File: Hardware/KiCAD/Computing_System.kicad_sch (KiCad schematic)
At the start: 7 parts, among them IC9 PCF8575PWR, J1 SD_Card, U1 ESP32-C3-WROOM-02

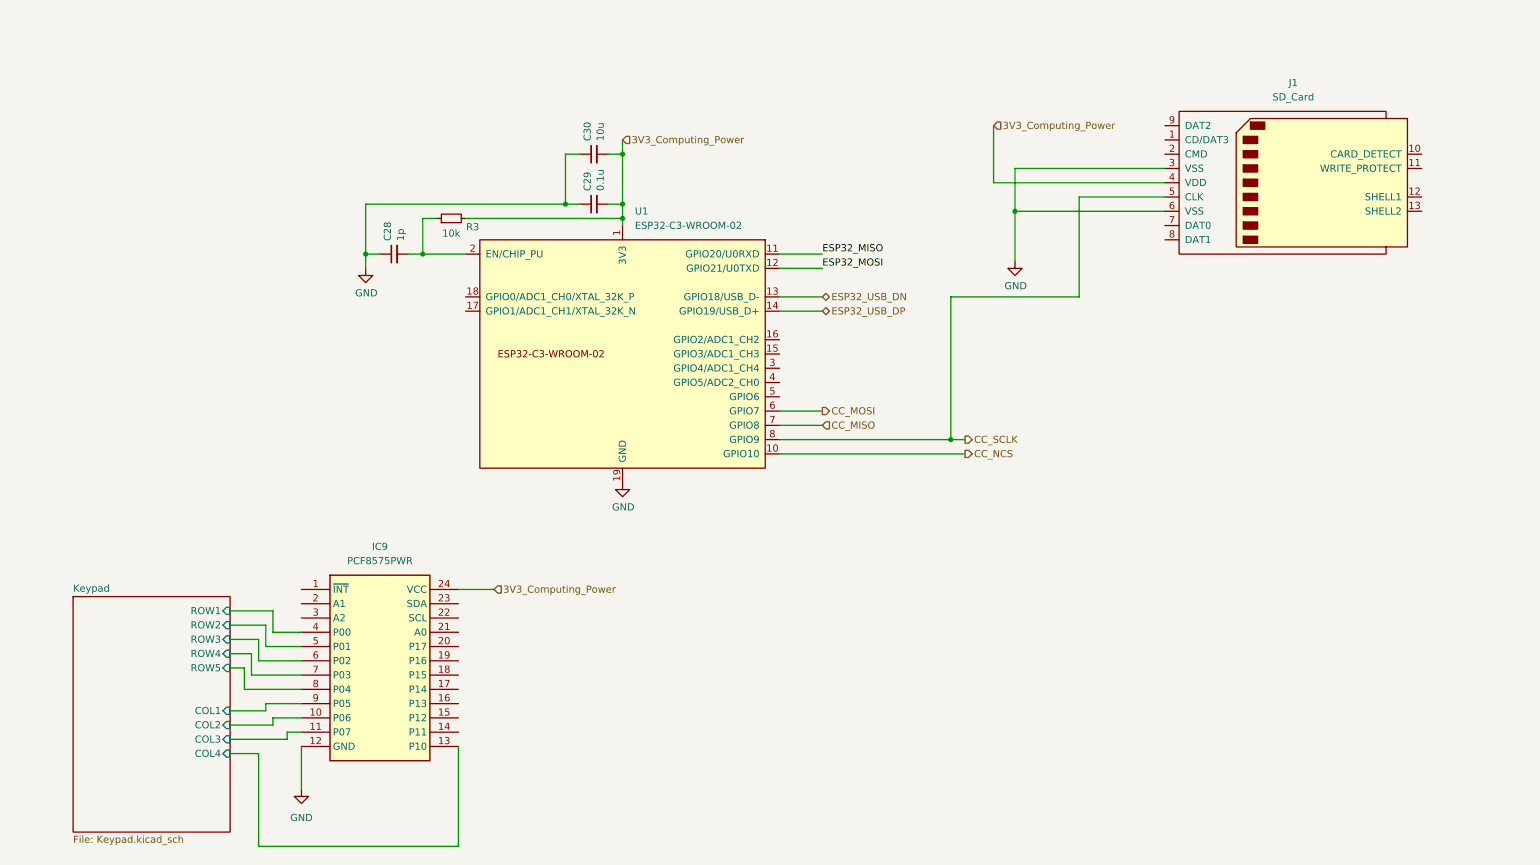
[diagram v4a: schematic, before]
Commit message: feat: subsystem exploration, begin placement, routing #11 #12 #4 many new project symbols
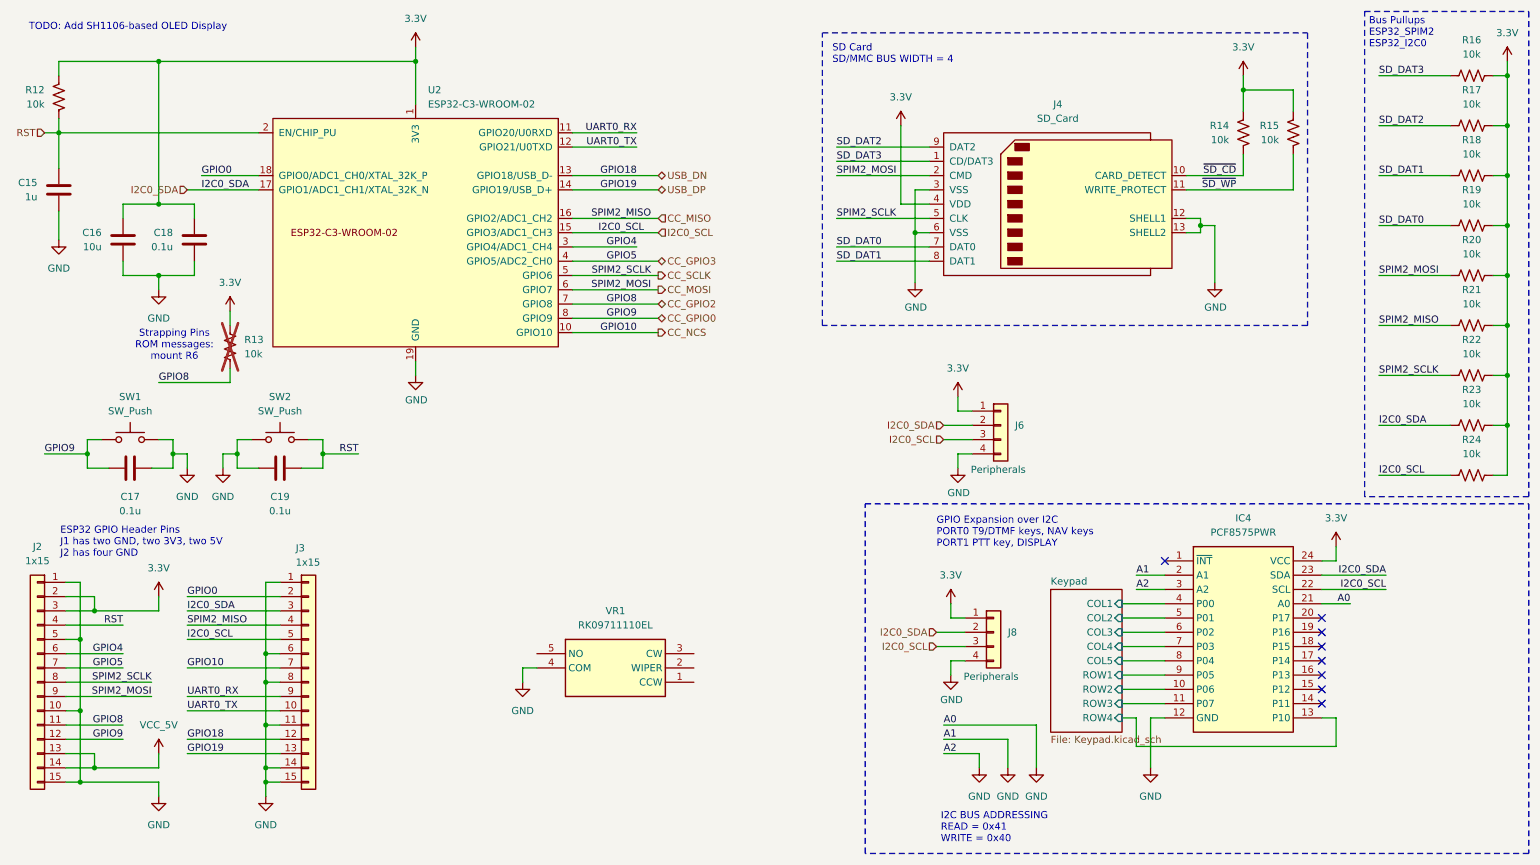
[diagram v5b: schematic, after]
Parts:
- removed C28: 1p, Capacitor_SMD:C_0402_1005Metric, symbol pkl_device:pkl_C_Small
- removed C29: 0.1u, Capacitor_SMD:C_0402_1005Metric, symbol pkl_device:pkl_C_Small
- removed C30: 10u, Capacitor_SMD:C_0402_1005Metric, symbol pkl_device:pkl_C_Small
- removed R3: 10k, Resistor_SMD:R_0402_1005Metric, symbol pkl_device:pkl_R_Small
- added C15: 1u, Capacitor_SMD:C_0603_1608Metric, symbol Device:C
- added C16: 10u, Capacitor_SMD:C_0603_1608Metric, symbol Device:C
- added C17, C18, C19: 0.1u, Capacitor_SMD:C_0603_1608Metric, symbol Device:C
- added J2, J3: 1x15, Connector_PinHeader_2.54mm:PinHeader_1x15_P2.54mm_Vertical, symbol Connector_Generic:Conn_01x15
- added J6, J8: Peripherals, Connector_JST:JST_EH_B4B-EH-A_1x04_P2.50mm_Vertical, symbol Connector_Generic:Conn_01x04
- added R12, R13, R14, R15, R16, R17, R18, R19, R20, R21, R22, R23, R24: 10k, Resistor_SMD:R_0603_1608Metric, symbol Device:R_US
- added SW1, SW2: SW_Push, Button_Switch_SMD:SW_SPST_CK_RS282G05A3, symbol Switch:SW_Push
- added VR1: RK09711110EL, Cobalt_Cowboy:RK09711110EL, symbol Cobalt-Cowboy:RK09711110EL
- renumbered IC9 to IC4, J1 to J4, U1 to U2
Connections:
- net CC_MISO: now also U2.16 (GPIO2/ADC1_CH2), J3.4 (Pin_4), R21.1; no longer U2.7 (GPIO8)
- net CC_MOSI: now also J4.2 (CMD), J2.9 (Pin_9), R20.1
- net CC_NCS: now also J3.7 (Pin_7)
- net CC_SCLK: now also U2.5 (GPIO6), J2.8 (Pin_8), R22.1; no longer U2.8 (GPIO9)
- net GND: now also IC4.2 (A1), IC4.21 (A0), IC4.3 (A2), J4.12 (SHELL1), J4.13 (SHELL2), C15.1, C16.2, C17.1, C18.1, C19.1, J2.1 (Pin_1), J2.10 (Pin_10), J2.15 (Pin_15), J2.5 (Pin_5), J3.1 (Pin_1), J3.11 (Pin_11), J3.14 (Pin_14), J3.15 (Pin_15), J3.6 (Pin_6), J3.8 (Pin_8), J6.4 (Pin_4), J8.4 (Pin_4), SW1.1, SW2.1, VR1.4 (COM)
- net Keypad/COL1: now also IC4.4 (P00); no longer IC4.9 (P05)
- net Keypad/COL2: now also IC4.5 (P01); no longer IC4.10 (P06)
- net Keypad/COL3: now also IC4.6 (P02); no longer IC4.11 (P07)
- net Keypad/COL4: now also IC4.7 (P03); no longer IC4.13 (P10)
- net Keypad/ROW1: now also IC4.9 (P05); no longer IC4.4 (P00)
- net Keypad/ROW2: now also IC4.10 (P06); no longer IC4.5 (P01)
- net Keypad/ROW3: now also IC4.11 (P07); no longer IC4.6 (P02)
- net Keypad/ROW4: now also IC4.13 (P10); no longer IC4.7 (P03)
- net SD_DAT3: now reaches J4.1 (CD/DAT3)
- net SD_DAT3: now also R16.1
- net ~{SD_CD}: now reaches J4.10 (CARD_DETECT)
- net ~{SD_CD}: now also R14.1
- net ~{SD_WP}: now reaches J4.11 (WRITE_PROTECT)
- net ~{SD_WP}: now also R15.1
- net SD_DAT0: now reaches J4.7 (DAT0)
- net SD_DAT0: now also R19.1
- net SD_DAT1: now reaches J4.8 (DAT1)
- net SD_DAT1: now also R18.1
- net SD_DAT2: now reaches J4.9 (DAT2)
- net SD_DAT2: now also R17.1
- net RST: now reaches U2.2 (EN/CHIP_PU)
- net RST: now also C15.2, C19.2, J2.4 (Pin_4), R12.1, SW2.2
- net I2C0_SCL: now reaches U2.15 (GPIO3/ADC1_CH3)
- net I2C0_SCL: now also IC4.22 (SCL), J3.5 (Pin_5), J6.3 (Pin_3), J8.3 (Pin_3), R24.2
- net I2C0_SDA: now reaches U2.17 (GPIO1/ADC1_CH1/XTAL_32K_N)
- net I2C0_SDA: now also IC4.23 (SDA), J3.3 (Pin_3), J6.2 (Pin_2), J8.2 (Pin_2), R23.2
- net GPIO0: now reaches U2.18 (GPIO0/ADC1_CH0/XTAL_32K_P)
- net GPIO0: now also J3.2 (Pin_2)
- net GPIO4: now reaches U2.3 (GPIO4/ADC1_CH4)
- net GPIO4: now also J2.6 (Pin_6)
- net CC_GPIO3: now reaches U2.4 (GPIO5/ADC2_CH0)
- net CC_GPIO3: now also J2.7 (Pin_7)
- net 3V3_Computing_Power renamed 3.3V
- net 3.3V: now also C16.1, C18.2, J2.2 (Pin_2), J2.3 (Pin_3), J6.1 (Pin_1), J8.1 (Pin_1), R12.2, R13.2, R14.2, R15.2, R16.2, R17.2, R18.2, R19.2, R20.2, R21.2, R22.2, R23.1, R24.1
- net ESP32_MISO renamed UART0_RX
- net UART0_RX: now also J3.9 (Pin_9)
- net ESP32_MOSI renamed UART0_TX
- net UART0_TX: now also J3.10 (Pin_10)
- net ESP32_USB_DN renamed USB_DN
- net USB_DN: now also J3.12 (Pin_12)
- net ESP32_USB_DP renamed USB_DP
- net USB_DP: now also J3.13 (Pin_13)
- net Keypad/ROW5 renamed Keypad/COL5
- new net CC_GPIO0: C17.2, J2.12 (Pin_12), SW1.2, U2.8 (GPIO9)
- new net CC_GPIO2: J2.11 (Pin_11), R13.1, U2.7 (GPIO8)
- new net VCC_5V: J2.13 (Pin_13), J2.14 (Pin_14)
- no-connect marks 0 -> 8
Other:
- sheet Keypad ports: added COL5; removed ROW5
- note added: "Bus Pullups ESP32_SPIM2 ESP32_I2C0"
- note added: "ESP32 GPIO Header Pins J1 has two GND, two 3V3, two 5V J2 has four GND"
- note added: "GPIO Expansion over I2C PORT0 T9/DTMF keys, NAV keys PORT1 PTT key, DISPLAY"
- note added: "I2C BUS ADDRESSING READ = 0x41 WRITE = 0x40"
- note added: "SD Card SD/MMC BUS WIDTH = 4"
- note added: "Strapping Pins ROM messages: mount R6"
- note added: "TODO: Add SH1106-based OLED Display"
- moved on the sheet: IC4, J4, U2
